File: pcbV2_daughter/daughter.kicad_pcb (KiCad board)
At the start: 2 copper layers, 92.5 x 75.4 mm, 29 parts, among them J3 Conn_01x03_Male, J6 Conn_01x03_Male

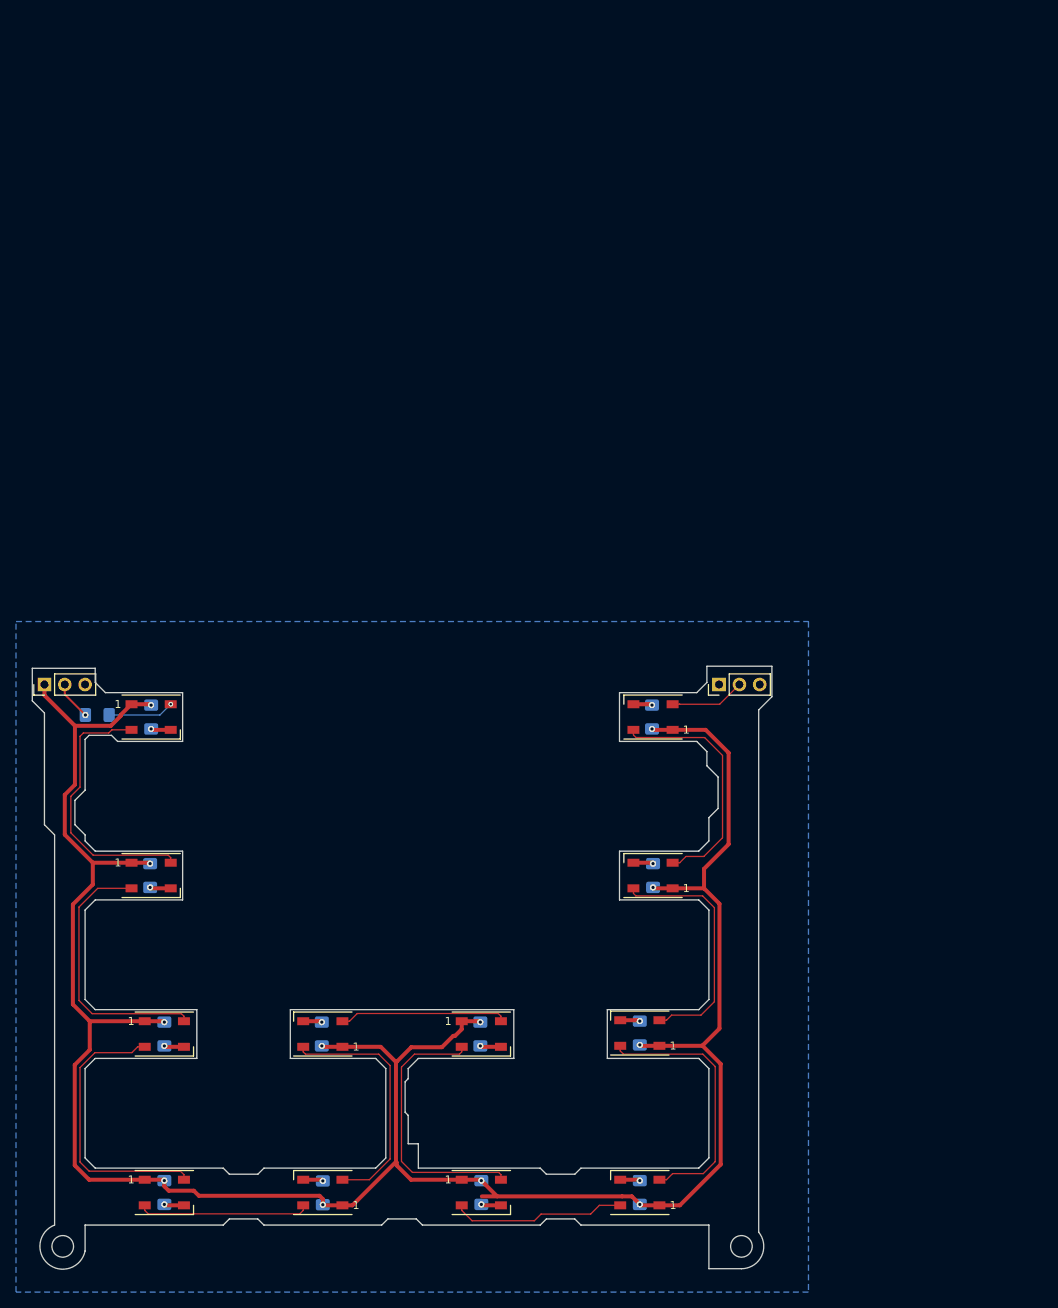
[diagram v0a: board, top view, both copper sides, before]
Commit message: Prototype 1 Code changes (#9)
* started working on low priority work thread

* removed usb c

* setup a low priority worker thread that we can assign a bunch of menial tasks to

* added dip switch support

* started rewiring

* v2 layout

* edited layout, updated daughter board

* moved some labels around

* generated plots files

* added the ability to enable, disable and delete threads by handler ID

* added thread safety to the low priority work thread

* added documentation for dip switches

* finished adding thread safety code, fixed SPI dma ram waste usage

* update

* updated gerber files

* moved over lpwork into it's own module

* added signature to the codebase

* added more signatures

* updating daughter board to be more structurally safe

* generated gerber files

Co-authored-by: Jonathan Low <jwlow@uci.edu>
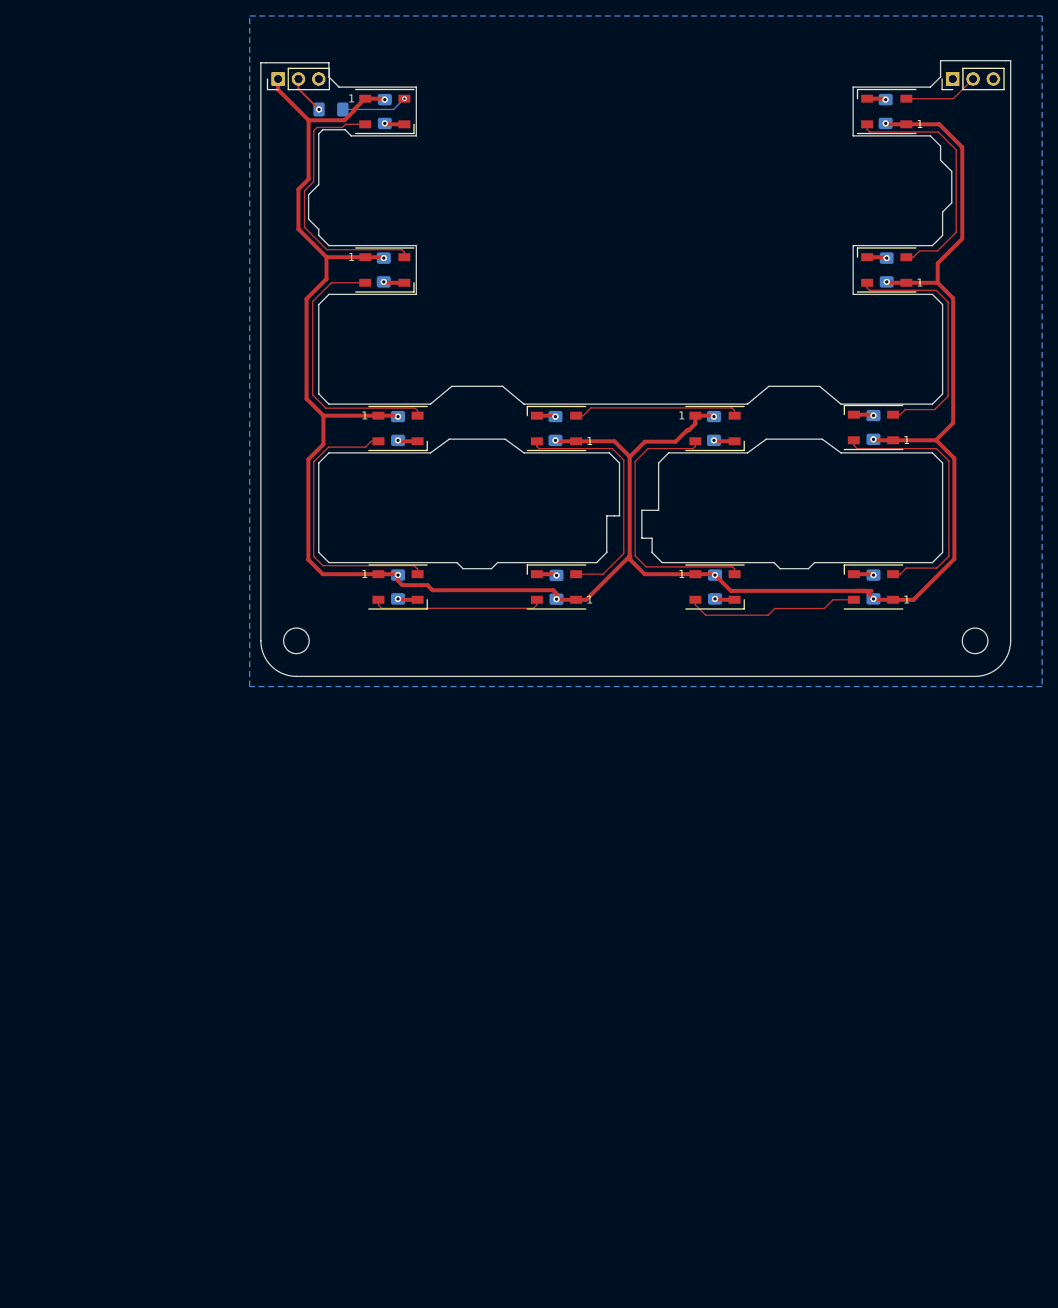
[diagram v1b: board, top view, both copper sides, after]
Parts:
- removed the REF** at (78.7, 189.4)
- removed the REF** at (163.6, 189.4)
- added REF**: MountingHole_3.2mm_M3, MountingHole:MountingHole_3.2mm_M3, F.Cu at (108.0, 113.7)
- added REF**: MountingHole_3.2mm_M3, MountingHole:MountingHole_3.2mm_M3, F.Cu at (192.8, 113.7)
- moved C1 81.1 mm to (120.7, 106.9)
- moved C10 81.1 mm to (181.7, 67.3)
- moved C11 81.1 mm to (180.1, 87.0)
- moved C12 81.1 mm to (180.1, 106.9)
- moved C3 81.1 mm to (118.9, 67.3)
- moved C4 81.1 mm to (119.0, 47.5)
- moved C7 81.1 mm to (160.3, 106.9)
- moved C9 81.1 mm to (181.6, 47.5)
- moved D14 81.1 mm to (120.7, 106.9)
- moved D16 81.1 mm to (119.0, 67.3)
- moved D17 81.1 mm to (119.0, 47.5)
- moved D18 81.1 mm to (160.3, 106.9)
- moved D21 81.1 mm to (140.5, 106.9)
- moved D22 81.1 mm to (181.7, 47.5)
- moved D23 81.1 mm to (181.7, 67.3)
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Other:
- board size 92.5 x 75.4 mm -> 93.7 x 77 mm
